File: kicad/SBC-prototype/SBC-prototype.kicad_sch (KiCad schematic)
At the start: 13 parts, among them IC1 W65C02S6TPG-14, SW1 SW_Push, Y1 ECS-2100AX-1.0MHZ

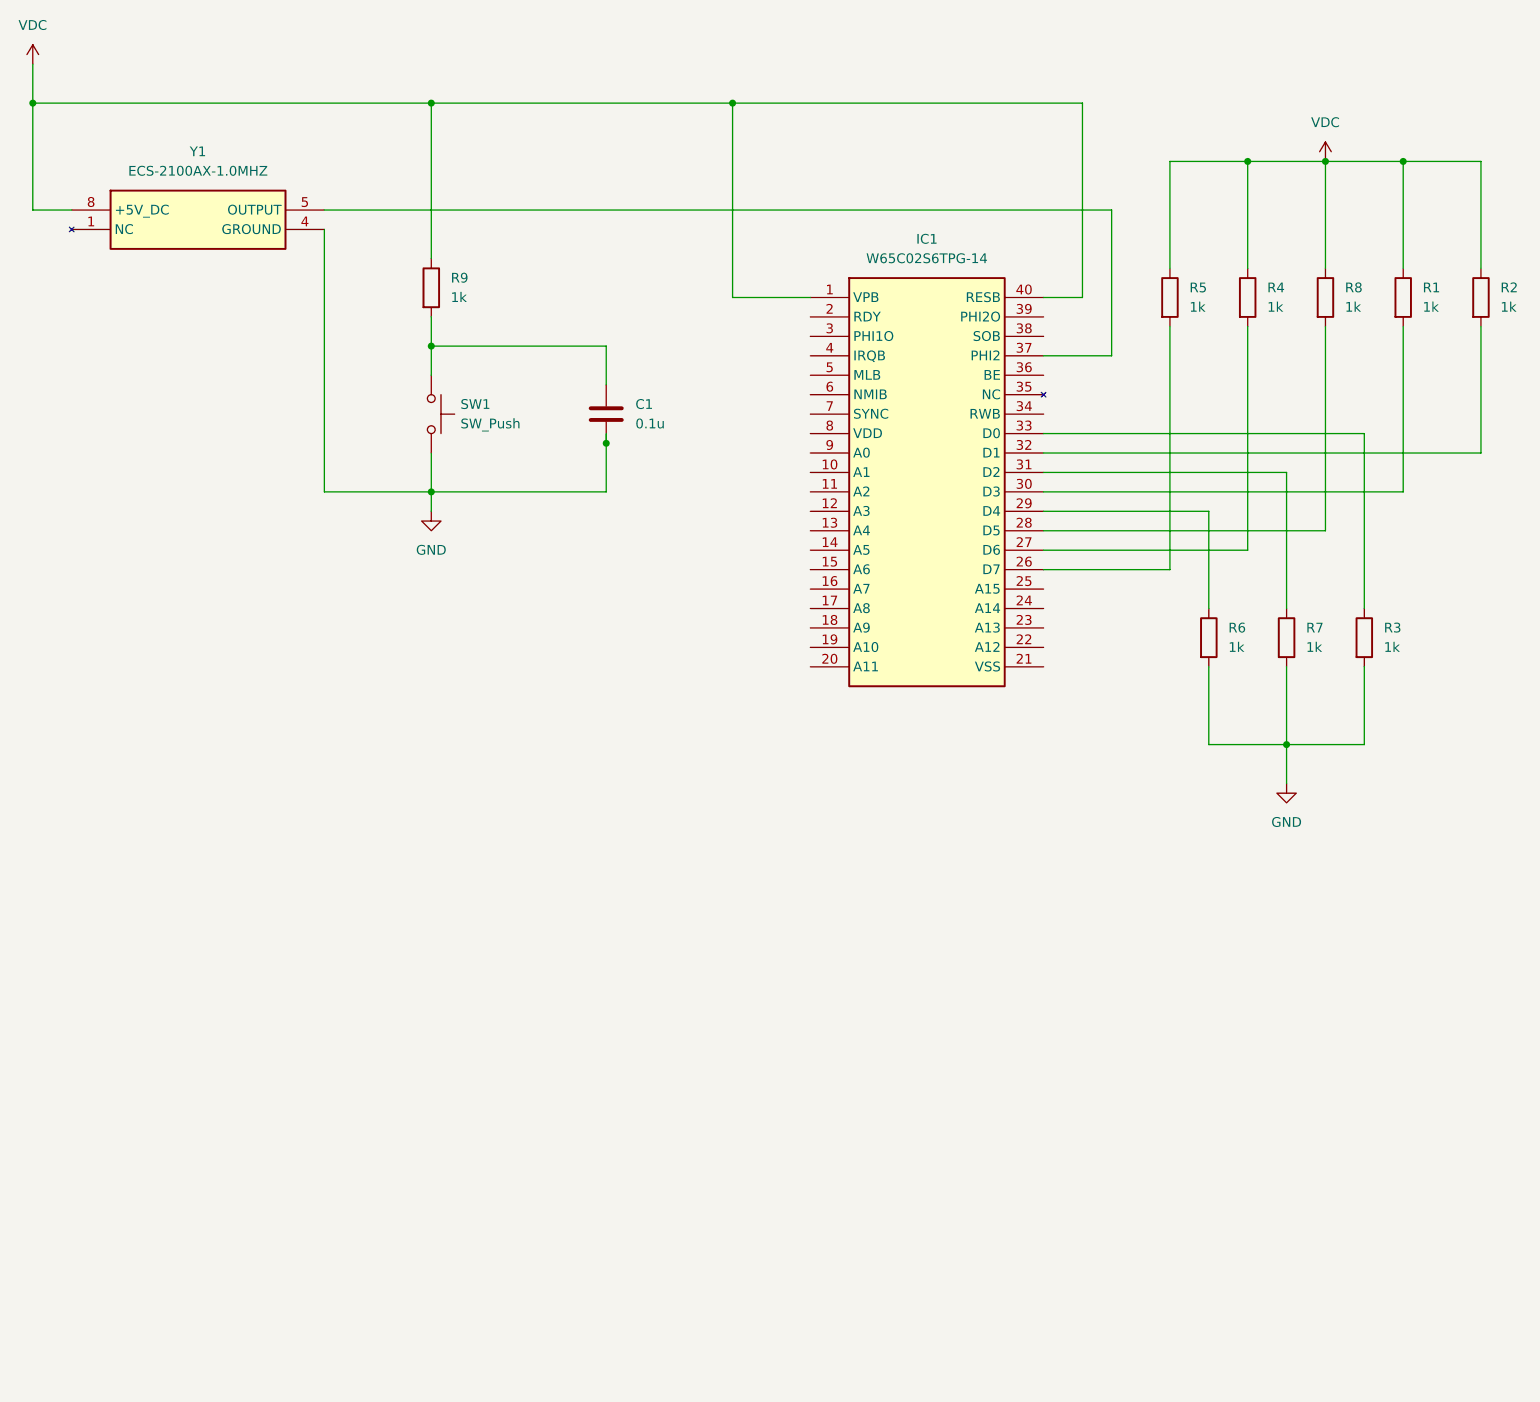
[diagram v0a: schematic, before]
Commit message: Adding power, ground, clocks, reset, and basic address decode logic.
- Need to specify exactly how the address decode logic is going to work
- Should decide how many VIA and UART I want on the Mk0 revision
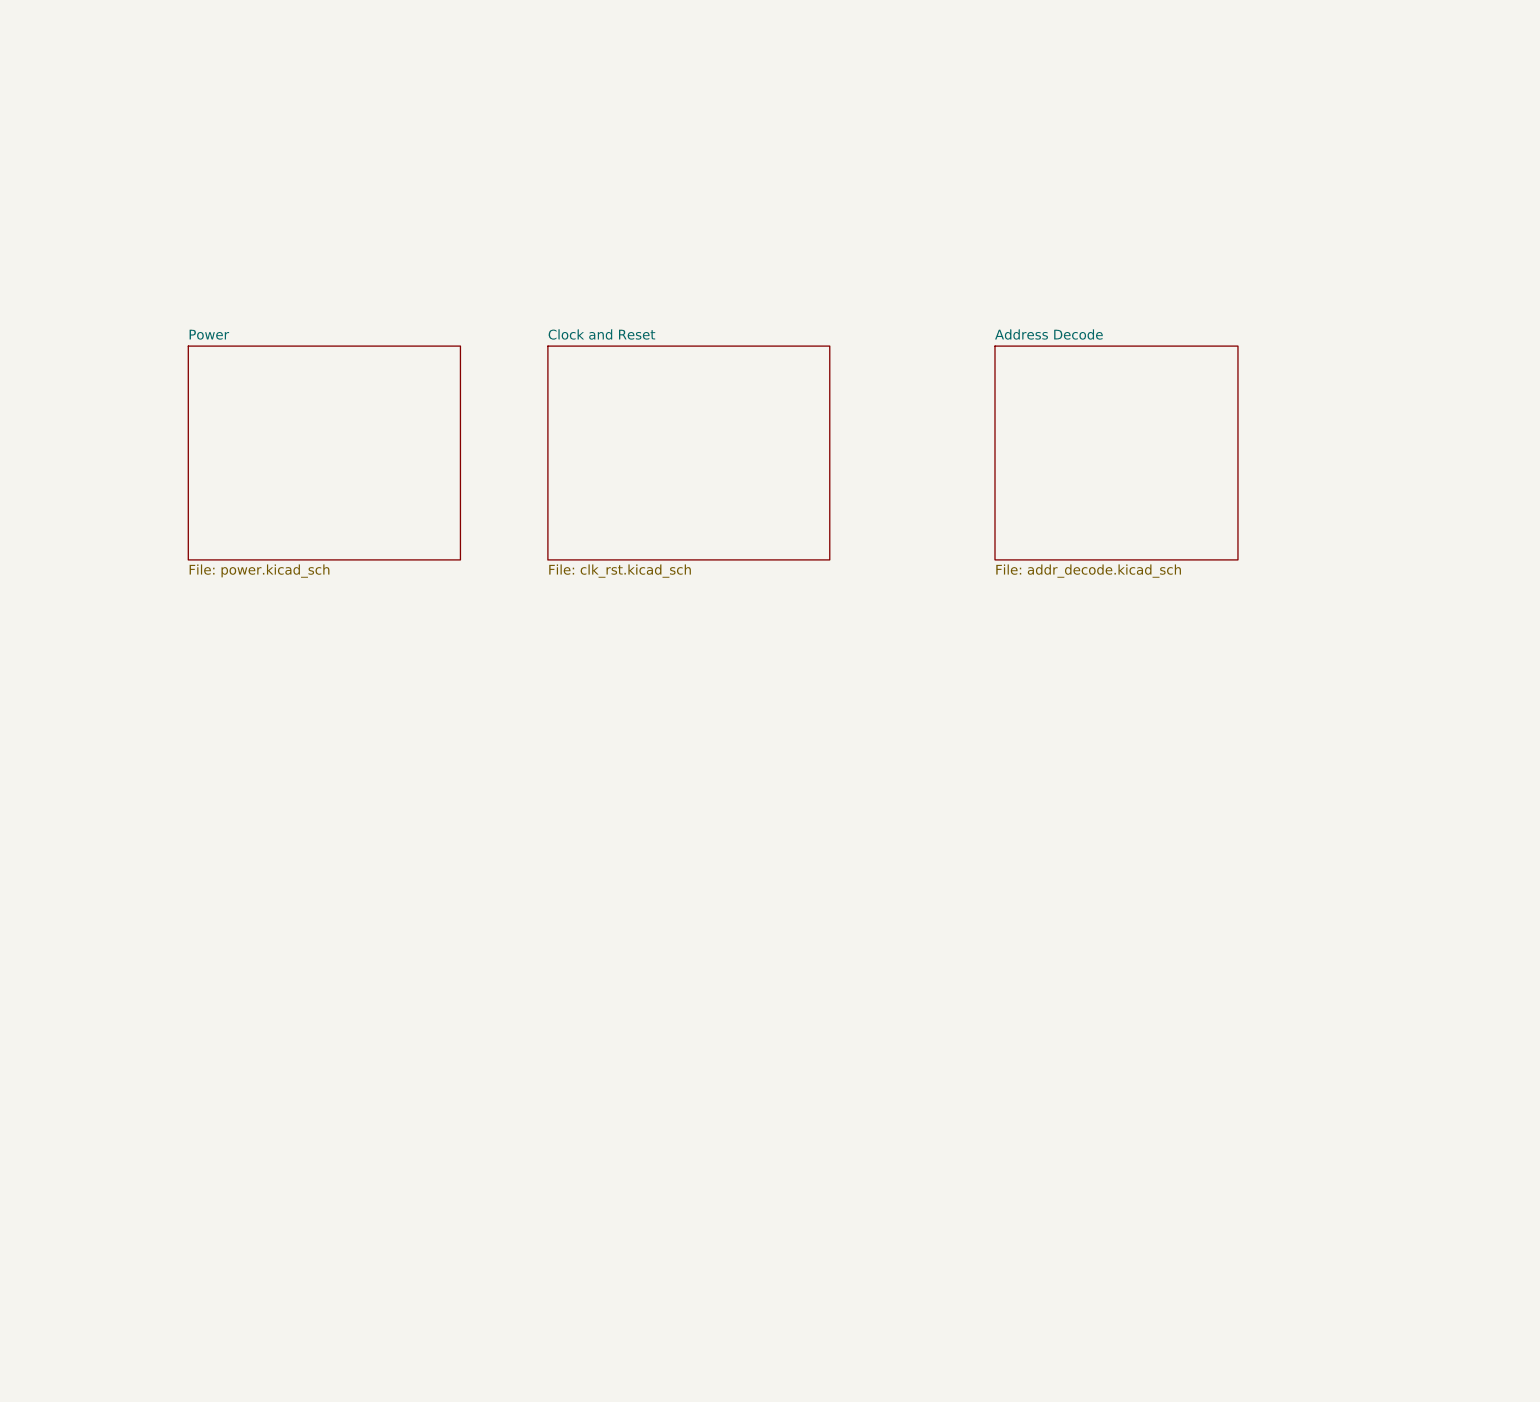
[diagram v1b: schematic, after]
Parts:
- removed C1: 0.1u, symbol Device:C
- removed IC1: W65C02S6TPG-14, DIP1524W56P254L5207H508Q40N, symbol 6502-sbc:W65C02S6TPG-14
- removed R1, R2, R3, R4, R5, R6, R7, R8, R9: 1k, symbol Device:R
- removed SW1: SW_Push, symbol Switch:SW_Push
- removed Y1: ECS-2100AX-1.0MHZ, ECS2100AX10MHZ, symbol 6502-sbc:ECS-2100AX-1.0MHZ
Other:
- added sheet Address Decode (addr_decode.kicad_sch)
- added sheet Clock and Reset (clk_rst.kicad_sch)
- added sheet Power (power.kicad_sch)
- title: (none) -> 65C02 Single Board Computer

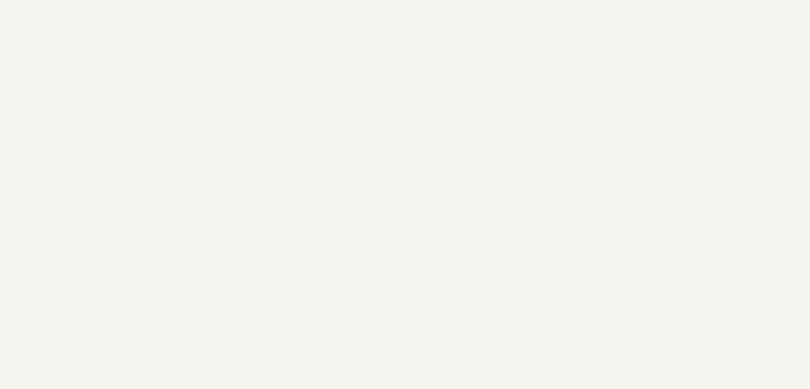
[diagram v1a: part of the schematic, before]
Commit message: Started on address decode logic. Need to finihs this tonight.
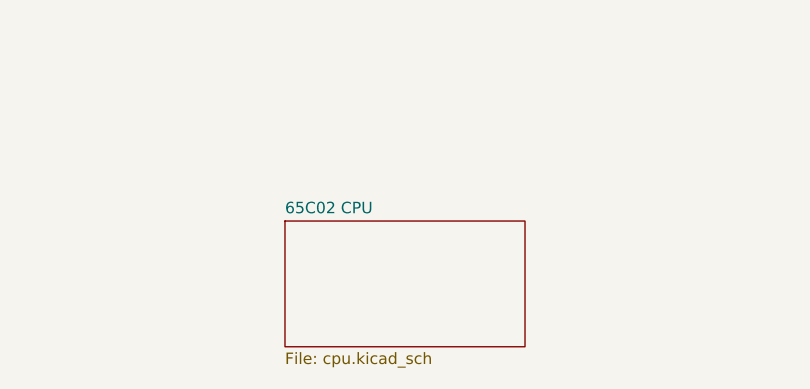
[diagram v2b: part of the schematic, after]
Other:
- added sheet 65C02 CPU (cpu.kicad_sch)
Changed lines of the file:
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@@
+	)
+	(sheet
+		(at 95.25 105.41)
+		(size 26.67 13.97)
+		(fields_autoplaced yes)
+		(stroke
+			(width 0.1524)
+			(type solid)
+		)
+		(fill
+			(color 0 0 0 0.0000)
+		)
+		(property "Sheetname" "65C02 CPU"
+			(at 95.25 104.6984 0)
+			(effects
+				(font
+					(size 1.27 1.27)
+				)
+				(justify left bottom)
+			)
+		)
+		(property "Sheetfile" "cpu.kicad_sch"
+			(at 95.25 119.9646 0)
+			(effects
+				(font
+					(size 1.27 1.27)
+				)
+				(justify left top)
+			)
+		)
+		(instances
+			(project "SBC-prototype"
+				(path "/1c8fb460-190a-4823-a6aa-9b1d397d6158"
+					(page "5")
+				)
+			)
+		)
 	)
 	(sheet

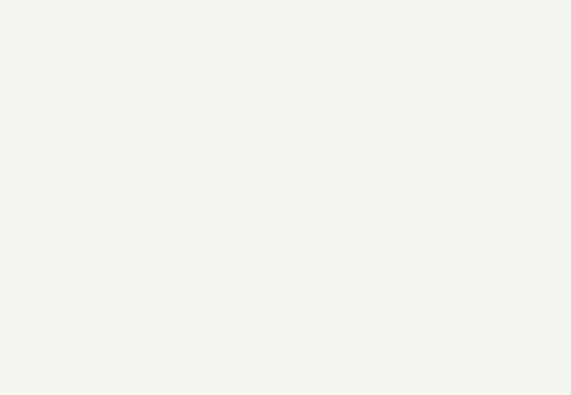
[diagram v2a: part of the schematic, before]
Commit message: Adding SRAM and EEPROM to schematic
- Also ignoring all Kicad backup .zip files
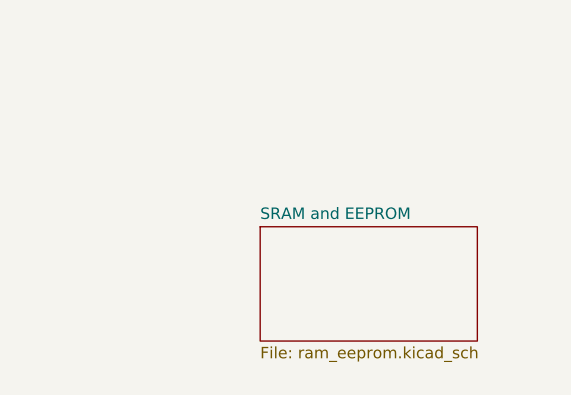
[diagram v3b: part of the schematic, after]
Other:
- added sheet SRAM and EEPROM (ram_eeprom.kicad_sch)
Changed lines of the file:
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@@
 	(title_block
 		(title "65C02 Single Board Computer")
-		(rev "-")
+		(rev "Mk. 0")
 	)
 	(sheet
@@
 				)
 			)
+		)
+	)
+	(sheet
+		(at 153.67 105.41)
+		(size 24.13 12.7)
+		(fields_autoplaced yes)
+		(stroke
+			(width 0.1524)
+			(type solid)
+		)
+		(fill
+			(color 0 0 0 0.0000)
+		)
+		(property "Sheetname" "SRAM and EEPROM"
+			(at 153.67 104.6984 0)
+			(effects
+				(font
+					(size 1.27 1.27)
+				)
+				(justify left bottom)
+			)
+		)
+		(property "Sheetfile" "ram_eeprom.kicad_sch"
+			(at 153.67 118.6946 0)
+			(effects
+				(font
+					(size 1.27 1.27)
+				)
+				(justify left top)
+			)
+		)
+		(instances
+			(project "SBC-prototype"
+				(path "/1c8fb460-190a-4823-a6aa-9b1d397d6158"
+					(page "6")
+				)
+			)

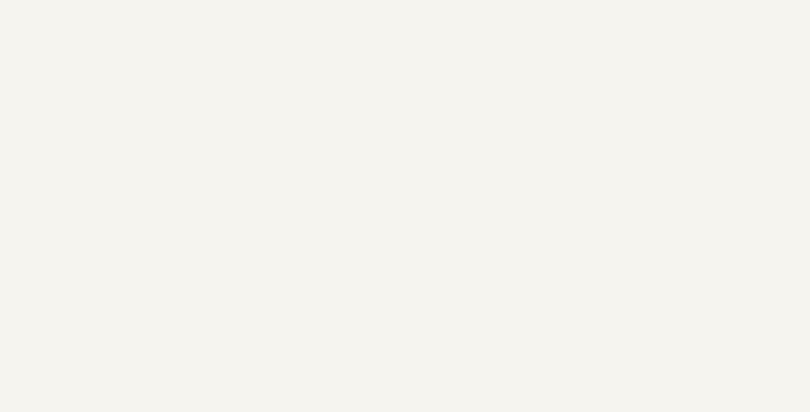
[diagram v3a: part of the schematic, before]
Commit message: Added a power LED, decoupling caps for the power supply and each IC
- Power supply now has a 100uF polarized cap on the 5V rail and 0.1uF
  caps on each of the IC power pins.
- Going to add a VIA to drive an LCD display and then build it
- Haven't looked at footprints yet
- Power input needs a SPDT power switch (I like the power switch like
  what is on the Xilinx FPGA eval boards).
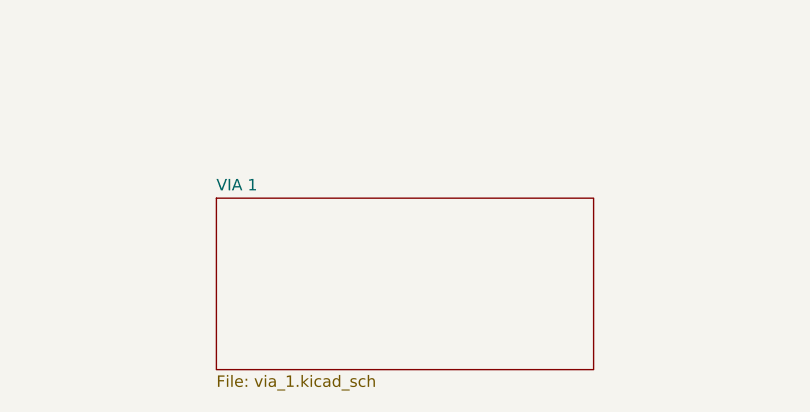
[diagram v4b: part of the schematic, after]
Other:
- added sheet VIA 1 (via_1.kicad_sch)
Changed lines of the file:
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@@
+	)
+	(sheet
+		(at 91.44 153.67)
+		(size 41.91 19.05)
+		(fields_autoplaced yes)
+		(stroke
+			(width 0.1524)
+			(type solid)
+		)
+		(fill
+			(color 0 0 0 0.0000)
+		)
+		(property "Sheetname" "VIA 1"
+			(at 91.44 152.9584 0)
+			(effects
+				(font
+					(size 1.27 1.27)
+				)
+				(justify left bottom)
+			)
+		)
+		(property "Sheetfile" "via_1.kicad_sch"
+			(at 91.44 173.3046 0)
+			(effects
+				(font
+					(size 1.27 1.27)
+				)
+				(justify left top)
+			)
+		)
+		(instances
+			(project "SBC-prototype"
+				(path "/1c8fb460-190a-4823-a6aa-9b1d397d6158"
+					(page "7")
+				)
+			)
+		)
 	)
 	(sheet
